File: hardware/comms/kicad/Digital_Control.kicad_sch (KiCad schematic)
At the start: 9 parts, among them J1 Conn_01x20, J2 Conn_01x20, J3 Conn_01x20

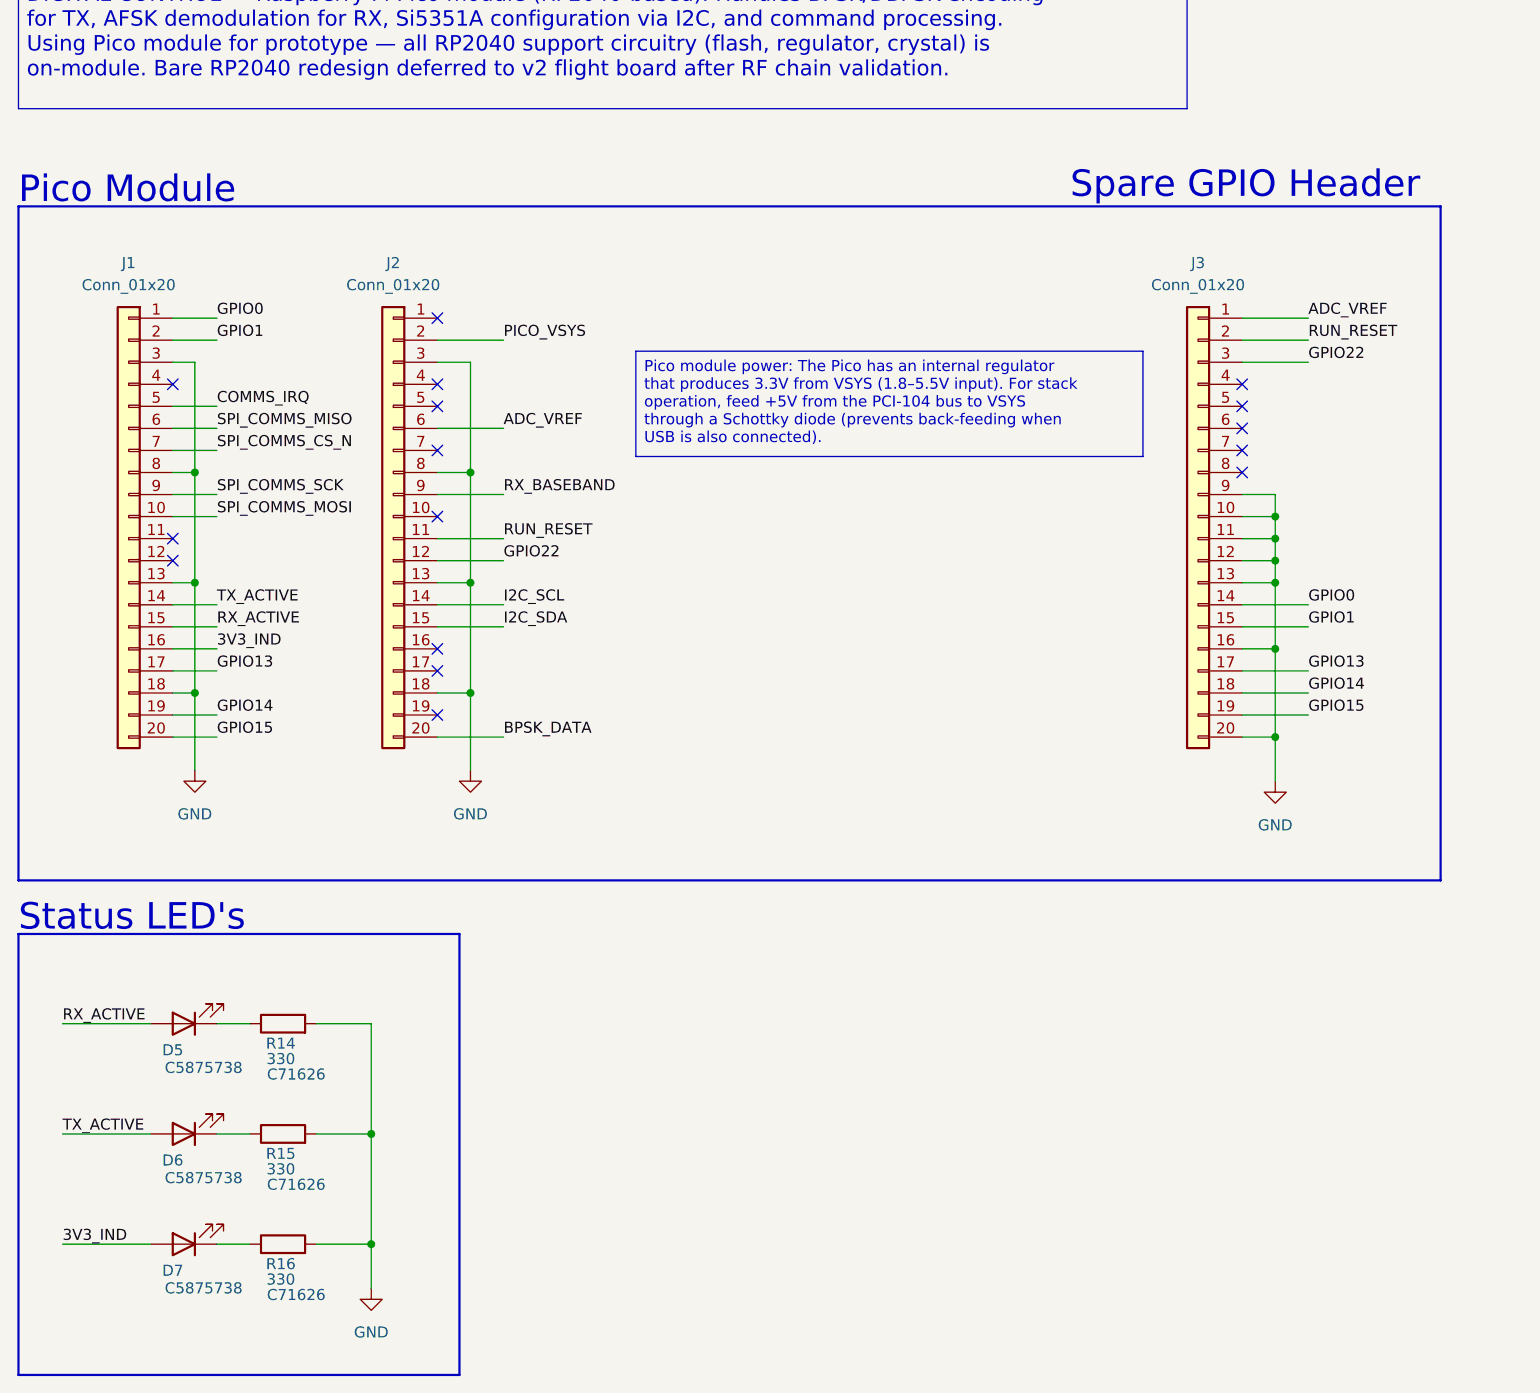
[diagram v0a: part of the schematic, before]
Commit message: comms/kicad: rename project and sheets, correct schematic text
  Renames
  - transciever_kicad.{pro,sch,pcb} -> transceiver.{pro,sch,pcb}: the
    project name was misspelled, and the _kicad suffix was redundant
    inside a kicad/ directory.
  - Sheet files lose their spaces: Clock_Gen, Digital_Control, RX_Chain,
    TX_Chain. Sheetname keeps its space -- that is the label drawn on the
    sheet, not a path.
  - References updated in four places, not one: 4 Sheetfile properties in
    the root schematic, 186 per-symbol (project ...) instances across every
    sheet, 68 per-footprint (sheetfile ...) entries in the PCB, and
    meta.filename plus the root sheet name in the project file. Verified
    afterwards that all sheet references resolve, no sheet is orphaned, and
    the project file still parses.

  Spelling and stale labels
  - Title block: Revsion -> Revision, Repsoitory -> Repository, repository
    path centisat -> ember, project named EMBER.
  - PCI-104 -> CSKB in three files. PCI-104 is a different real standard,
    and the same sheet's own revision history records the bus being renamed
    to CSKB back at rev 0.4.
  - Status LED's -> Status LEDs; +20 db -> +20 dB; RX SMA < - -> <-.
  - The tripler note named BRF92A as the flight transistor: misspelled, and
    superseded by the 2SC3356 actually placed. Corrected to 2SC3356 with
    the MMBT3904-footprint note the implementation plan records. The
    ft=5 GHz figure is dropped rather than reassigned to a part it was not
    measured against.
  - Power sheet: the D4 forward-drop note referred to the SA612, replaced
    by the ADE-1+ back at rev 0.5. Now names the PSA4-5043+.
 Altium-to-KiCad text damage
  Three separate corruptions, classified before replacing so that real
  values were not caught up in it -- ~21 dB and ~20 dB both contain a
  literal ~2 and would have been mangled by a blind pass.
  - 144 table column separators rendered as literal ~2; now |, so the
    sheet index, rail summary, net c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
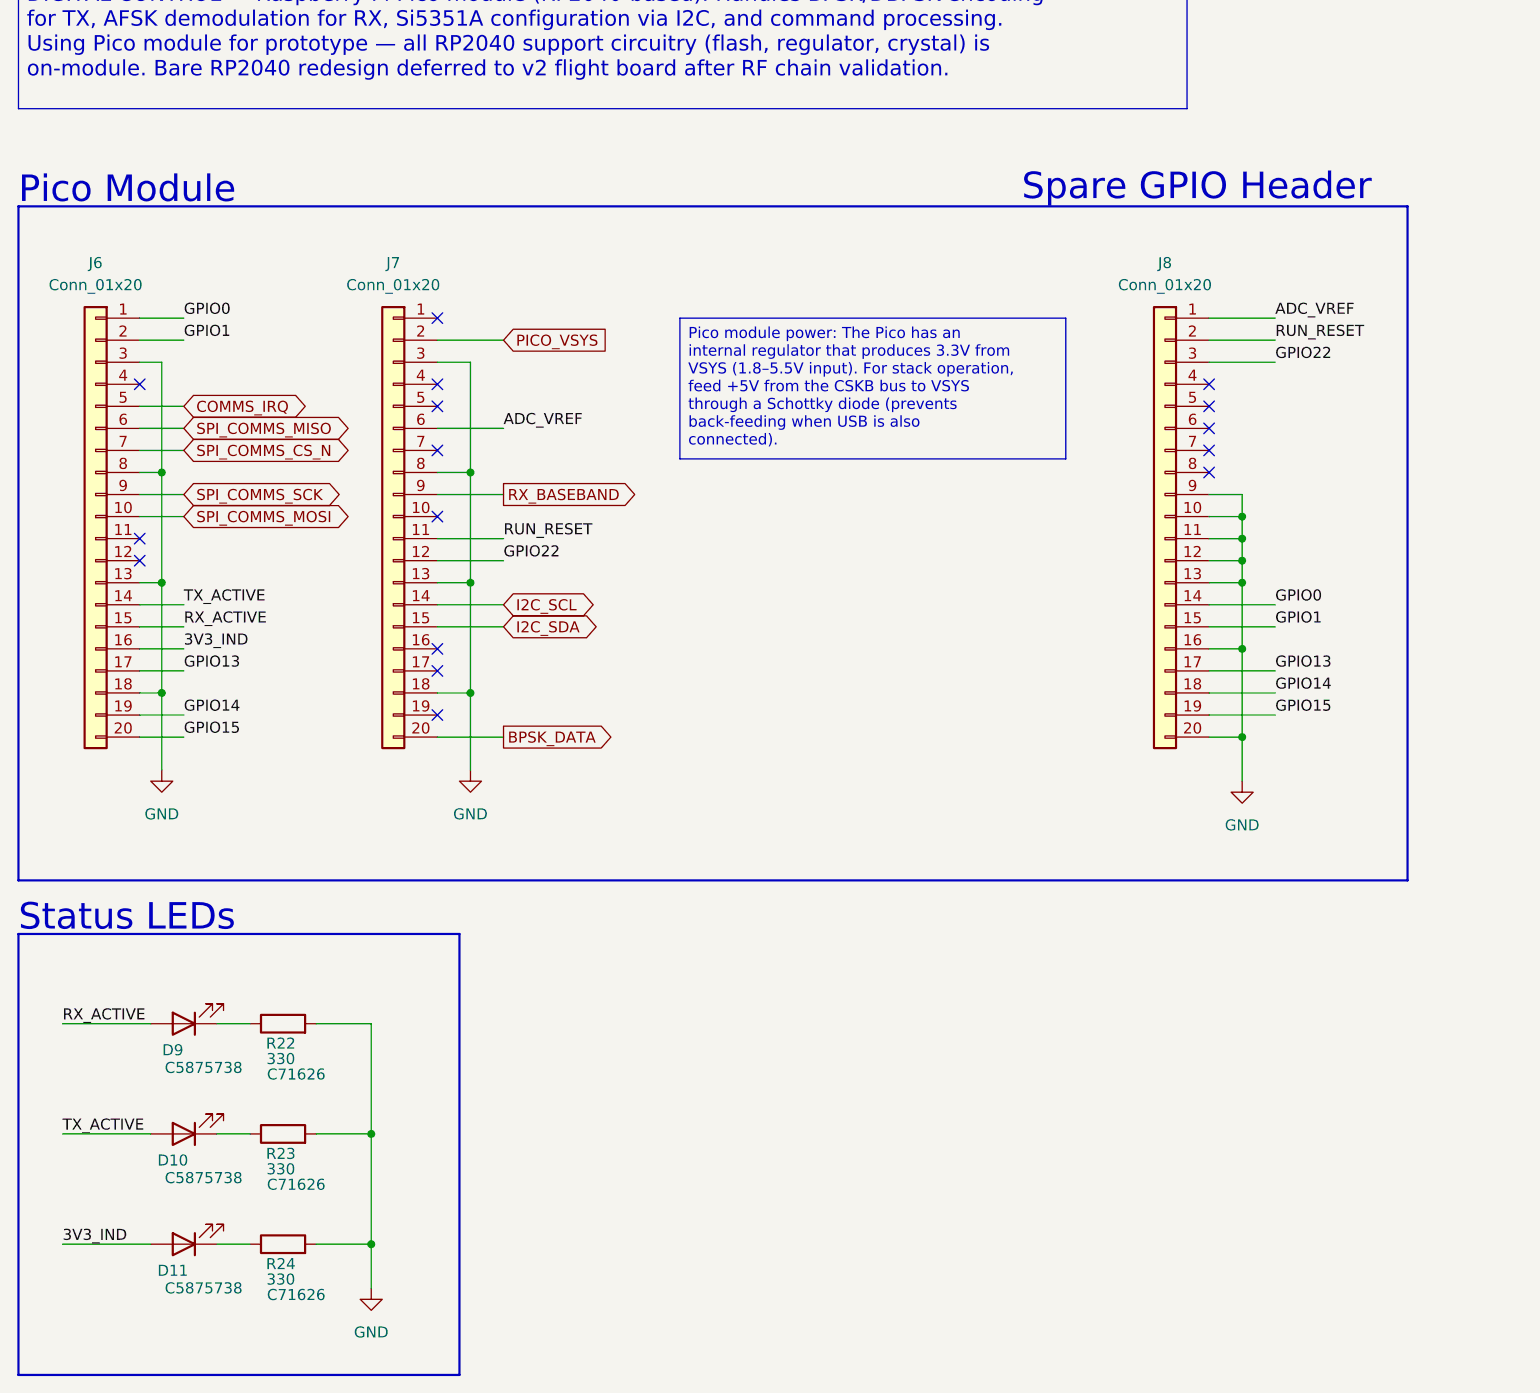
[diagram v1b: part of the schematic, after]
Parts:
- renumbered D6 to D10, D7 to D11, D5 to D9, J1 to J6, J2 to J7, J3 to J8, R14 to R22, R15 to R23, R16 to R24
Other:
- note added: "Status LEDs"
- note removed: "Status LED's"
- moved on the sheet: J6, J8

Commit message: Checkpoint comms PCB synchronization and connector alignment
Repair schematic-to-PCB links and apply the native update. Standardize J6/J7/J8 as DNP headers, align CSKB sockets for top-side assembly, and record pad-mapping verification.

Pre-RF-layout checkpoint: retain legacy circuitry for reviewed cleanup. Latest DRC has 631 errors, 273 warnings, and 140 unconnected items; board is not fabrication-ready.
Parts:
- J6, J7: footprint (none) -> Connector_PinHeader_2.54mm:PinHeader_1x20_P2.54mm_Vertical; AssemblyNote (none) -> DNP - optional 1x20 2.54mm through-hole header; do not popu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; LCSC Part # ESQ-120-14-G-S -> (none); now not fitted
- J8: footprint (none) -> Connector_PinHeader_2.54mm:PinHeader_1x20_P2.54mm_Vertical; Assembly Note (none) -> DNP - optional 1x20 2.54mm through-hole expansion header; p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; AssemblyNote (none) -> DNP - optional 1x20 2.54mm through-hole header; do not popu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; LCSC Part # ESQ-120-14-G-S -> (none); now not fitted
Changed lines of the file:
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@@
 		(on_board yes)
 		(in_pos_files yes)
-		(dnp no)
+		(dnp yes)
 		(fields_autoplaced yes)
 		(property "Reference" "J6"
@@
 			)
 		)
-		(property "Footprint" ""
+		(property "Footprint" "Connector_PinHeader_2.54mm:PinHeader_1x20_P2.54mm_Vertical"
 			(at 64.77 104.14 0)
 			(hide yes)
@@
 			)
 		)
-		(property "LCSC Part #" "ESQ-120-14-G-S"
+		(property "LCSC Part #" ""
+			(at 64.77 104.14 0)
+			(hide yes)
+			(show_name no)
+			(do_not_autoplace no)
+			(effects
+				(font
+					(size 1.27 1.27)
+				)
+			)
+		)
+		(property "MPN" ""
+			(at 64.77 104.14 0)
+			(hide yes)
+			(show_name no)
+			(do_not_autoplace no)
+			(effects
+				(font
+					(size 1.27 1.27)
+				)
+			)
+		)
+		(property "Manufacturer" ""
+			(at 64.77 104.14 0)
+			(hide yes)
+			(show_name no)
+			(do_not_autoplace no)
+			(effects
+				(font
+					(size 1.27 1.27)
+				)
+			)
+		)
+		(property "AssemblyNote" "DNP - optional 1x20 2.54mm through-hole header; do not populate at assembly"
 			(at 64.77 104.14 0)
 			(hide yes)
@@
 		(on_board yes)
 		(in_pos_files yes)
-		(dnp no)
+		(dnp yes)
 		(fields_autoplaced yes)
 		(property "Reference" "J8"
@@
 			)
 		)
-		(property "Footprint" ""
+		(property "Footprint" "Connector_PinHeader_2.54mm:PinHeader_1x20_P2.54mm_Vertical"
 			(at 187.96 104.14 0)
 			(hide yes)
@@
 			)
 		)
-		(property "LCSC Part #" "ESQ-120-14-G-S"
+		(property "LCSC Part #" ""
+			(at 187.96 104.14 0)
+			(hide yes)
+			(show_name no)
+			(do_not_autoplace no)
+			(effects
+				(font
+					(size 1.27 1.27)
+				)
+			)
+		)
+		(property "Assembly Note" "DNP - optional 1x20 2.54mm through-hole expansion header; populate only for future use"
+			(at 187.96 104.14 0)
+			(hide yes)
+			(show_name no)
+			(do_not_autoplace no)
+			(effects
+				(font
+					(size 1.27 1.27)
+				)
+			)
+		)
+		(property "AssemblyNote" "DNP - optional 1x20 2.54mm through-hole header; do not populate at assembly"
+			(at 187.96 104.14 0)
+			(hide yes)
+			(show_name no)
+			(do_not_autoplace no)
+			(effects
+				(font
+					(size 1.27 1.27)
+				)
+			)
+		)
+		(property "MPN" ""
+			(at 187.96 104.14 0)
+			(hide yes)
+			(show_name no)
+			(do_not_autoplace no)
+			(effects
+				(font
+					(size 1.27 1.27)
+				)
+			)
+		)
+		(property "Manufacturer" ""
 			(at 187.96 104.14 0)
 			(hide yes)
@@
 		(on_board yes)
 		(in_pos_files yes)
-		(dnp no)
+		(dnp yes)
 		(fields_autoplaced yes)
 		(property "Reference" "J7"
@@
 			)
 		)
-		(property "Footprint" ""
+		(property "Footprint" "Connector_PinHeader_2.54mm:PinHeader_1x20_P2.54mm_Vertical"
 			(at 99.06 104.14 0)
 			(hide yes)
@@
 			)
 		)
-		(property "LCSC Part #" "ESQ-120-14-G-S"
+		(property "LCSC Part #" ""
 			(at 99.06 104.14 0)
 			(hide yes)
+			(show_name no)
+			(do_not_autoplace no)
+			(effects
+				(font
+					(size 1.27 1.27)
+				)
+			)
+		)
+		(property "MPN" ""
+			(at 99.06 104.14 0)
+			(hide yes)
+			(show_name no)
+			(do_not_autoplace no)
+			(effects
+				(font
+					(size 1.27 1.27)
+				)
+			)
+		)
+		(property "Manufacturer" ""
+			(at 99.06 104.14 0)
+			(hide yes)
+			(show_name no)
+			(do_not_autoplace no)
+			(effects
+				(font
+					(size 1.27 1.27)
+				)
+			)
+		)
+		(property "AssemblyNote" "DNP - optional 1x20 2.54mm through-hole header; do not populate at assembly"
+			(at 99.06 104.14 0)
+			(hide yes)

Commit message: Checkpoint validated single-antenna comms routing before placement optimization
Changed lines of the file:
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@@
-		)
-	)
-	(label "TX_ACTIVE"
-		(at 74.93 114.3 0)
-		(effects
-			(font
-				(size 1.27 1.27)
-			)
-			(justify left bottom)
 		)
 	)
@@
 		)
 	)
-	(label "TX_ACTIVE"
-		(at 60.96 175.26 0)
-		(effects
-			(font
-				(size 1.27 1.27)
-			)
-			(justify left bottom)
-		)
-	)
 	(global_label "SPI_COMMS_CS_N"
 		(shape bidirectional)
 		(at 74.93 96.52 0)
-		(fields_autoplaced yes)
 		(effects
 			(font
@@
 		(shape input)
 		(at 111.76 83.82 0)
-		(fields_autoplaced yes)
 		(effects
 			(font
@@
 		(shape output)
 		(at 111.76 129.54 0)
-		(fields_autoplaced yes)
 		(effects
 			(font
@@
 		(shape bidirectional)
 		(at 74.93 101.6 0)
-		(fields_autoplaced yes)
 		(effects
 			(font
@@
 		(shape bidirectional)
 		(at 111.76 114.3 0)
-		(fields_autoplaced yes)
 		(effects
 			(font
@@
 		)
 	)
+	(global_label "TX_ACTIVE"
+		(shape output)
+		(at 74.93 114.3 0)
+		(effects
+			(font
+				(size 1.27 1.27)
+			)
+			(justify left)
+		)
+		(property "Intersheetrefs" "${INTERSHEET_REFS}"
+			(at 74.93 114.3 0)
+			(hide yes)
+			(show_name no)
+			(do_not_autoplace no)
+			(effects
+				(font
+					(size 1.27 1.27)
+				)
+			)
+		)
+	)
+	(global_label "TX_ACTIVE"
+		(shape output)
+		(at 60.96 175.26 180)
+		(effects
+			(font
+				(size 1.27 1.27)
+			)
+			(justify right)
+		)
+		(property "Intersheetrefs" "${INTERSHEET_REFS}"
+			(at 60.96 175.26 0)
+			(hide yes)
+			(show_name no)
+			(do_not_autoplace no)
+			(effects
+				(font
+					(size 1.27 1.27)
+				)
+			)
+		)
+	)
 	(global_label "SPI_COMMS_MISO"
 		(shape bidirectional)
 		(at 74.93 93.98 0)
-		(fields_autoplaced yes)
 		(effects
 			(font
@@
 		(shape bidirectional)
 		(at 111.76 116.84 0)
-		(fields_autoplaced yes)
 		(effects
 			(font
@@
 		(shape output)
 		(at 111.76 101.6 0)
-		(fields_autoplaced yes)
 		(effects
 			(font
@@
 		(shape bidirectional)
 		(at 74.93 91.44 0)
-		(fields_autoplaced yes)
 		(effects
 			(font
@@
 		(shape bidirectional)
 		(at 74.93 104.14 0)
-		(fields_autoplaced yes)
-		(effects
-			(font
+		(effects
+			(font

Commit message: progress on comms board
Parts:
- added C8, C9: 100nF, Capacitor_SMD:C_0805_2012Metric, symbol Device:C_Small
- added JP1, JP2: Jumper_2_Open, Connector_PinHeader_2.54mm:PinHeader_1x02_P2.54mm_Vertical, symbol Jumper:Jumper_2_Open
- added R5, R6: 120R, Resistor_SMD:R_0805_2012Metric, symbol Device:R
- added U2, U3: SN65HVD230, Package_SO:SOIC-8_3.9x4.9mm_P1.27mm, symbol Interface_CAN_LIN:SN65HVD230
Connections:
- net GND: now also C8.2, C9.2, U2.2 (GND), U2.8 (Rs), U3.2 (GND), U3.8 (Rs)
- net GPIO14: no longer J6.19 (Pin_19)
- net GPIO15: no longer J6.20 (Pin_20)
- net CAN_A_TX: now reaches J7.16 (Pin_16)
- net CAN_A_TX: now also U2.1 (D)
- net CAN_A_RX: now reaches J7.17 (Pin_17)
- net CAN_A_RX: now also U2.4 (R)
- net COMMS_IRQ: no longer names the net of J6.5 (Pin_5)
- net SPI_COMMS_CS_N: no longer names the net of J6.7 (Pin_7)
- net SPI_COMMS_MISO: no longer names the net of J6.6 (Pin_6)
- net SPI_COMMS_MOSI: no longer names the net of J6.10 (Pin_10)
- net SPI_COMMS_SCK: no longer names the net of J6.9 (Pin_9)
- new net: JP1.1 (A), R5.2
- new net: JP2.1 (A), R6.2
- new net CAN_A_H: R5.1, U2.7 (CANH)
- new net CAN_A_L: JP1.2 (B), U2.6 (CANL)
- new net CAN_B_H: R6.1, U3.7 (CANH)
- new net CAN_B_L: JP2.2 (B), U3.6 (CANL)
- new net CAN_B_RX: J6.19 (Pin_19), U3.4 (R)
- new net CAN_B_TX: J6.20 (Pin_20), U3.1 (D)
- new net VCC_3V3: C8.1, C9.1, U2.3 (VCC), U3.3 (VCC)
- no-connect marks 16 -> 21
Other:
- note added: "CAN Transceivers"
